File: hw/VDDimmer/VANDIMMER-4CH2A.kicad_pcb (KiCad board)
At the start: 2 copper layers, 100 x 80 mm, 96 parts, among them J1 USB-C 16P, J10 A2 V+SEL VIN/5V, J11 BTN1, J12 BTN2, J13 EXP 3V3/GND/SDA/SCL/EN/IO0, J14 UART1 3V3/GND/TX/RX, J2 VIN 9-24V, J3 CH1 V+/LED-, J4 CH2 V+/LED-, J5 CH3 V+/LED-, J6 CH4 V+/LED-, J7 ADDR1 V+/D/CLK/GND, J8 ADDR2 V+/D/CLK/GND, J9 A1 V+SEL VIN/5V, Q1 20N06, Q2 20N06, Q3 20N06, Q4 20N06, Q5 SUD50P06-15, U1 ESP32-S3-WROOM-1U-N16, U2 AP63301WU-7, U3 AMS1117-3.3, U4 74HCT125, U5 74HCT125

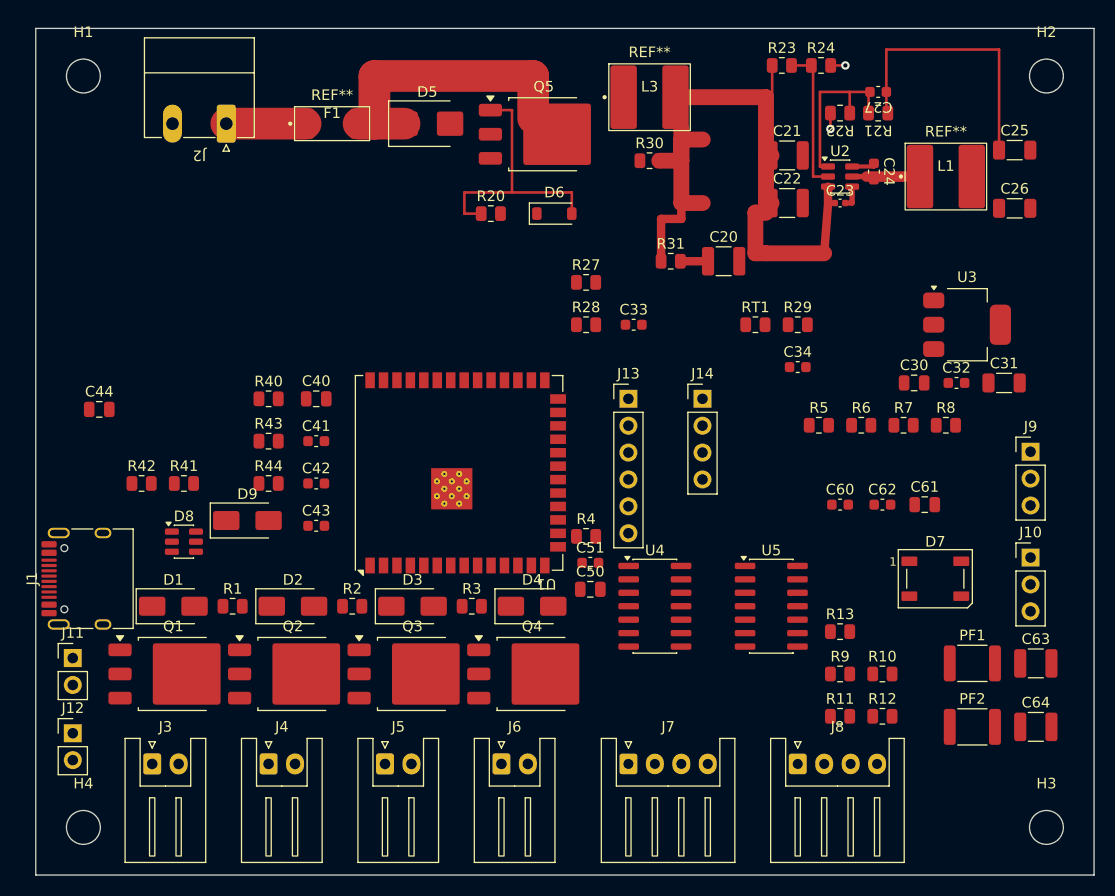
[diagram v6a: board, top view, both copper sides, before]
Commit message: Re-place U1 and R1-R8 to open the two routing bottlenecks
U1 moved 2.5 mm north, (140,102) -> (140,99.5). Nothing was routed to it and
the band x 126..154 / y 84..92.8 was empty, so the move is free. Effect on the
corridor between U1's bottom-row pads and the D1-D4 pad row:
  before: y 111.20..113.70 = 2.50 mm =  5 lanes; 7 traces needed at x=140
  after : y 108.70..113.70 = 5.00 mm = 10 lanes
The cut east of U1 at x=149.6 likewise widens from 6 to 12 lanes.

R1-R4 (220R series gate) moved into the D-row slots directly above each FET
gate, all rot 0 so GDRV lands on the west pad and GATE leaves on the east pad:
  R2 -> (118.6,114.6)  above Q2 gate x=119.26
  R3 -> (129.9,114.6)  above Q3 gate x=130.56
  R4 -> (141.2,114.6)  above Q4 gate x=141.86
  R1 -> (111.2,111.5) rot 180, north of D1, serving Q1 gate x=107.96
This makes GDRV1-4 four nested westward runs with zero forced crossings; the
previous arrangement interleaved every GDRV_n with GATE_n+1.

R5-R8 (10k gate pulldown) moved from (174..186, 97.5) -- 45 to 66 mm from the
gates they hold down -- into the 2.19 mm band between the Q courtyards
(y<=124.5) and the JST courtyards (y>=126.69), one directly below each FET at
y=125.6. Each now reaches its gate through the 2.0 mm channel beside that FET's
tab, 0.875 mm clearance either side.

DRC 0 errors, 0 phantom pads, unconnected 190. The 12 new warnings are all
silkscreen reference-designator overlaps, deferred to a silk pass.

Co-Authored-By: Claude Opus 5 (1M context) <noreply@anthropic.com>
Claude-Session: https://claude.ai/code/session_01XeXr1isxVCg8kRo5Eh8BHM
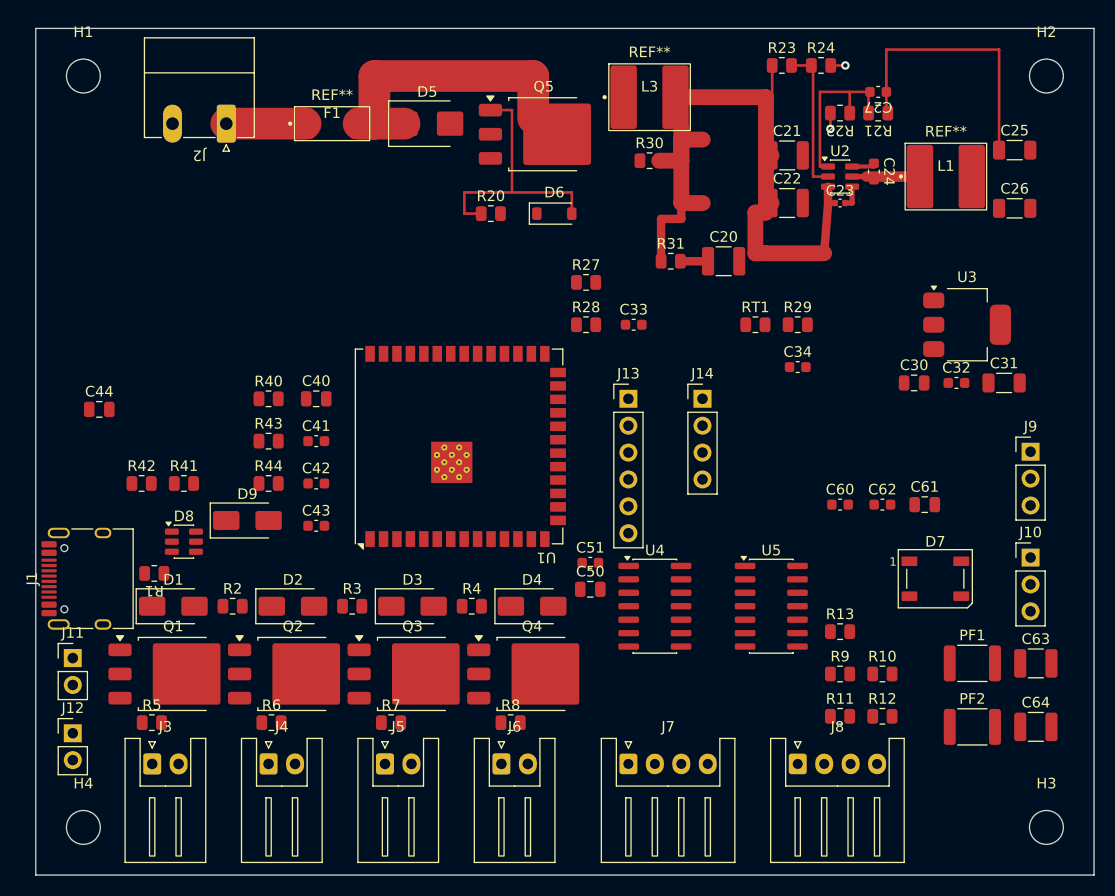
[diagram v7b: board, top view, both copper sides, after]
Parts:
- moved R5 69.0 mm to (111.0, 125.6)
- moved R6 62.4 mm to (122.3, 125.6)
- moved R7 56.0 mm to (133.6, 125.6)
- moved R8 49.8 mm to (144.9, 125.6)
- moved R4 12.7 mm to (141.2, 114.6)
- moved R2 11.3 mm to (118.6, 114.6)
- moved R3 11.3 mm to (129.9, 114.6)
- moved R1 8.02 mm to (111.2, 111.5), turned to 180 degrees
- moved U1 2.50 mm to (140.0, 99.5)
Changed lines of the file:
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@@
 	(footprint "Resistor_SMD:R_0805_2012Metric"
 		(layer "F.Cu")
-		(at 174 97.5)
+		(at 110.973 125.6)
 		(descr "Resistor SMD 0805 (2012 Metric), square (rectangular) end terminal, IPC-7351 nominal, (Body size source: IPC-SM-782 page 72, https://www.pcb-3d.com/wordpress/wp-content/uploads/ipc-sm-782a_amendment_1_and_2.pdf)")
 		(tags "resistor")
@@
 	(footprint "Resistor_SMD:R_0805_2012Metric"
 		(layer "F.Cu")
-		(at 141.2 114.6)
+		(at 129.9 114.6)
 		(descr "Resistor SMD 0805 (2012 Metric), square (rectangular) end terminal, IPC-7351 nominal, (Body size source: IPC-SM-782 page 72, https://www.pcb-3d.com/wordpress/wp-content/uploads/ipc-sm-782a_amendment_1_and_2.pdf)")
 		(tags "resistor")
@@
 	(footprint "Resistor_SMD:R_0805_2012Metric"
 		(layer "F.Cu")
-		(at 178 97.5)
+		(at 122.273 125.6)
 		(descr "Resistor SMD 0805 (2012 Metric), square (rectangular) end terminal, IPC-7351 nominal, (Body size source: IPC-SM-782 page 72, https://www.pcb-3d.com/wordpress/wp-content/uploads/ipc-sm-782a_amendment_1_and_2.pdf)")
 		(tags "resistor")
@@
 	(footprint "Resistor_SMD:R_0805_2012Metric"
 		(layer "F.Cu")
-		(at 186 97.5)
+		(at 144.873 125.6)
 		(descr "Resistor SMD 0805 (2012 Metric), square (rectangular) end terminal, IPC-7351 nominal, (Body size source: IPC-SM-782 page 72, https://www.pcb-3d.com/wordpress/wp-content/uploads/ipc-sm-782a_amendment_1_and_2.pdf)")
 		(tags "resistor")
@@
 	(footprint "Resistor_SMD:R_0805_2012Metric"
 		(layer "F.Cu")
-		(at 152 108)
+		(at 141.2 114.6)
 		(descr "Resistor SMD 0805 (2012 Metric), square (rectangular) end terminal, IPC-7351 nominal, (Body size source: IPC-SM-782 page 72, https://www.pcb-3d.com/wordpress/wp-content/uploads/ipc-sm-782a_amendment_1_and_2.pdf)")
 		(tags "resistor")
@@
 	(footprint "Resistor_SMD:R_0805_2012Metric"
 		(layer "F.Cu")
-		(at 129.9 114.6)
+		(at 118.6 114.6)
 		(descr "Resistor SMD 0805 (2012 Metric), square (rectangular) end terminal, IPC-7351 nominal, (Body size source: IPC-SM-782 page 72, https://www.pcb-3d.com/wordpress/wp-content/uploads/ipc-sm-782a_amendment_1_and_2.pdf)")
 		(tags "resistor")
@@
 	(footprint "Resistor_SMD:R_0805_2012Metric"
 		(layer "F.Cu")
-		(at 118.6 114.6)
+		(at 111.2 111.5 180)
 		(descr "Resistor SMD 0805 (2012 Metric), square (rectangular) end terminal, IPC-7351 nominal, (Body size source: IPC-SM-782 page 72, https://www.pcb-3d.com/wordpress/wp-content/uploads/ipc-sm-782a_amendment_1_and_2.pdf)")
 		(tags "resistor")
 		(property "Reference" "R1"
-			(at 0 -1.649999 0)
+			(at 0 -1.649999 180)
 			(unlocked yes)
 			(layer "F.SilkS")
@@
 		)
 		(property "Value" "220R"
-			(at 0 1.65 0)
+			(at 0 1.65 180)
 			(unlocked yes)
 			(layer "F.SilkS")
@@
 		)
 		(property "Datasheet" ""
-			(at 0 0 0)
+			(at 0 0 180)
 			(layer "F.Fab")
 			(hide yes)
@@
 		)
 		(property "Description" ""
-			(at 0 0 0)
+			(at 0 0 180)
 			(layer "F.Fab")
 			(hide yes)
@@
 		)
 		(property "KiLib_Generator" "SMD_2terminal_chip_molded"
-			(at 0 0 0)
+			(at 0 0 180)
 			(layer "F.SilkS")
 			(hide yes)
@@
 		(duplicate_pad_numbers_are_jumpers no)
 		(fp_line
-			(start -0.227064 -0.735)
-			(end 0.227064 -0.735)
+			(start -0.227064 0.735)
+			(end 0.227064 0.735)
 			(stroke
 				(width 0.12)
@@
 		)
 		(fp_line
-			(start -0.227064 0.735)
-			(end 0.227064 0.735)
+			(start -0.227064 -0.735)
+			(end 0.227064 -0.735)
 			(stroke
 				(width 0.12)
@@
 		)
 		(fp_text user "${REFERENCE}"
-			(at 0 0 0)
+			(at 0 0 180)
 			(unlocked yes)
 			(layer "F.Fab")
@@
 		)
 		(pad "1" smd roundrect
-			(at -0.9125 0)
+			(at -0.9125 0 180)
 			(size 1.025 1.4)
 			(layers "F.Cu" "F.Mask" "F.Paste")
@@
 		)
 		(pad "2" smd roundrect
-			(at 0.9125 0)
+			(at 0.9125 0 180)
 			(size 1.025 1.4)
 			(layers "F.Cu" "F.Mask" "F.Paste")
@@
 	(footprint "Resistor_SMD:R_0805_2012Metric"
 		(layer "F.Cu")
-		(at 182 97.5)
+		(at 133.573 125.6)
 		(descr "Resistor SMD 0805 (2012 Metric), square (rectangular) end terminal, IPC-7351 nominal, (Body size source: IPC-SM-782 page 72, https://www.pcb-3d.com/wordpress/wp-content/uploads/ipc-sm-782a_amendment_1_and_2.pdf)")
 		(tags "resistor")
@@
 	(footprint "RF_Module:ESP32-S3-WROOM-1U"
 		(layer "F.Cu")
-		(at 140 102 90)
+		(at 140 99.5 90)
 		(descr "2.4 GHz Wi-Fi and Bluetooth module  https://www.espressif.com/sites/default/files/documentation/esp32-s3-wroom-1_wroom-1u_datasheet_en.pdf")
 		(tags "2.4 GHz Wi-Fi and Bluetooth module")

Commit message: Route the whole PWM chain: U1 -> U4 -> R1-R4 -> Q1-Q4, drains, pulldowns
GATE_IN1-4 reach U4 through the 3.0 mm gap between the SOIC-14's two pad
columns (x 157.0..160.0), descending on lanes x = 157.6/158.1/158.6/159.1.
That is what makes the section planar: the 74HCT125 alternates input and
output on each side, so inputs arriving from the west and outputs leaving to
the west must cross. Bringing all four inputs down the package centre leaves
U4's west pads free for GDRV1/GDRV2 to exit west and its east pads free for
GDRV3/GDRV4 to exit east. Zero crossings, zero bottom-layer traces.

GDRV1-4 run west on four nested corridor lanes y = 111.2/111.7/112.2/112.7,
dropping at x = 112.112/117.688/128.988/140.287 onto R1-R4. Lane pitch 0.5 mm,
edge-to-edge gap 0.25 mm; nearest obstacle above is U1's pad row at y 108.7
(0.375 mm) and below D1-D4 at y 113.7 (0.875 mm).

GATE1-4 leave R1-R4 into each FET's gate pad, then continue down the 2.0 mm
channel beside that FET's tab to the pulldown below it: 0.875 mm clearance
to the gate pad on one side and the tab on the other.

DRAIN1-4 at 1.0 mm (spec 8.4), two segments each: flyback cathode to FET tab,
then tab to the JST pin. Descents offset to x = 114.0/125.0/136.0/147.3 to keep
0.5 mm or more from each pulldown's ground pad.

C50/C51 moved from (152.4, 110.5/113) -- where they blocked the U4 fan-out
channel entirely -- to (164, 108.5/111), putting the 100 nF 2.25 mm from U4's
VCC pin instead of 9 mm.

DRC 0 errors, 0 phantom pads, unconnected 190 -> 166.

Co-Authored-By: Claude Opus 5 (1M context) <noreply@anthropic.com>
Claude-Session: https://claude.ai/code/session_01XeXr1isxVCg8kRo5Eh8BHM
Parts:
- moved C50 12.4 mm to (164.0, 108.5)
- moved C51 11.6 mm to (164.0, 111.0)
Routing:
- net /PWM/GDRV3: track 0.00 -> 48.6 mm
- net /PWM/GDRV2: track 0.00 -> 46.7 mm
- net /PWM/GDRV1: track 0.00 -> 46.0 mm
- net /PWM/GDRV4: track 0.00 -> 43.1 mm
- net GATE_IN3: track 0.00 -> 28.6 mm
- net GATE_IN4: track 0.00 -> 26.1 mm
- net GATE_IN2: track 0.00 -> 24.1 mm
- net /PWM/GATE1: track 0.00 -> 17.4 mm
- net GATE_IN1: track 0.00 -> 15.4 mm
- net /PWM/DRAIN4: track 0.00 -> 14.9 mm
- net /PWM/DRAIN3: track 0.00 -> 14.9 mm
- net /PWM/DRAIN2: track 0.00 -> 14.9 mm
- net /PWM/DRAIN1: track 0.00 -> 14.9 mm
- net /PWM/GATE3: track 0.00 -> 12.8 mm
- net /PWM/GATE2: track 0.00 -> 12.8 mm
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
